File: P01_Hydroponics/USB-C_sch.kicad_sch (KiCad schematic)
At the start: 24 parts, among them J7 USB_C_Receptacle_USB2.0_16P, Q3 PMOS, Q4 PMOS

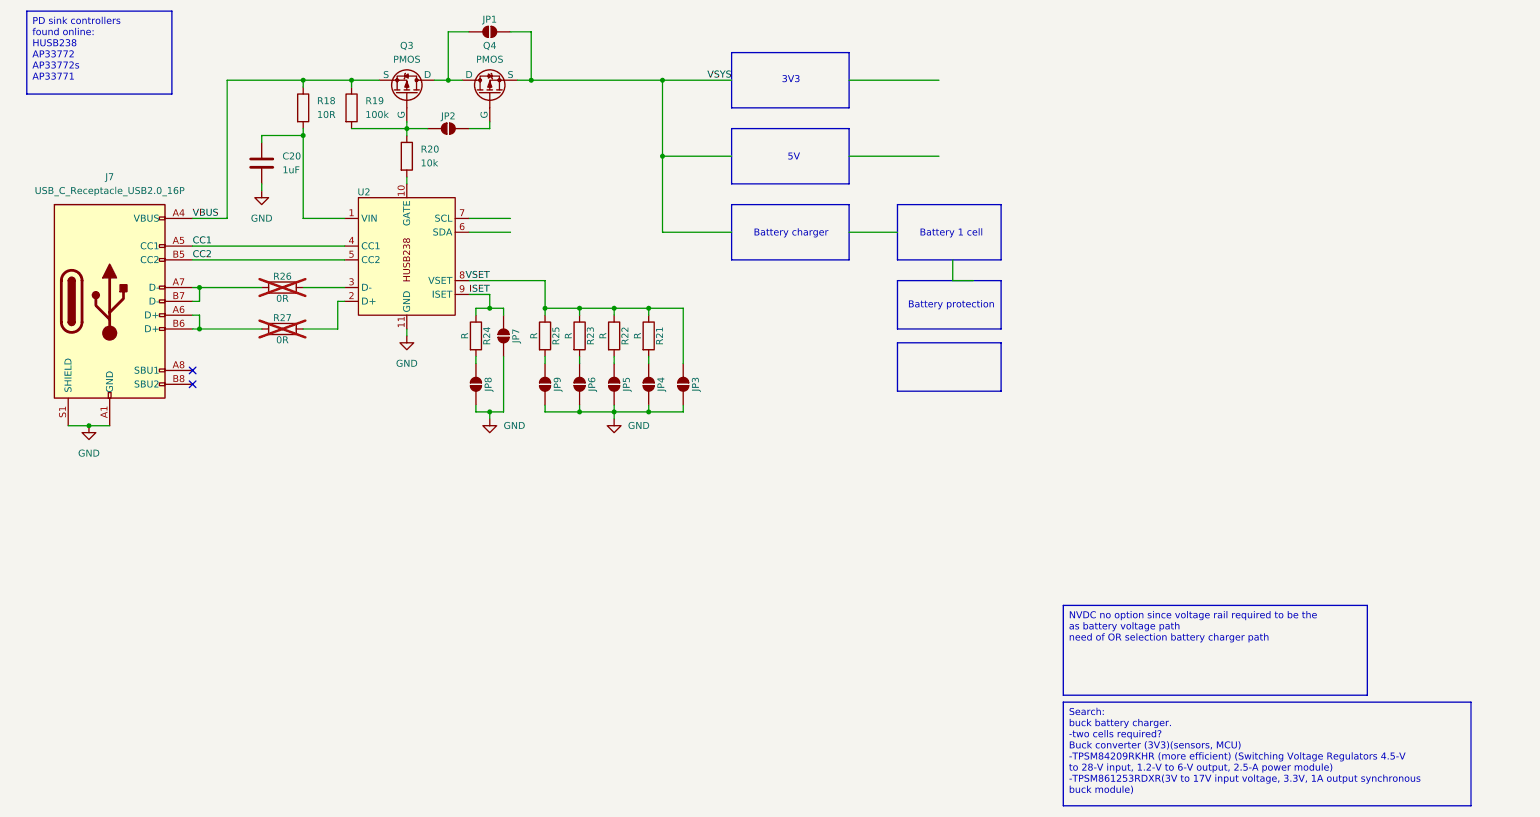
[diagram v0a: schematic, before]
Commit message: New version
Modified PD sink controller, and added 3v3 and 5V DC-DC buck converters
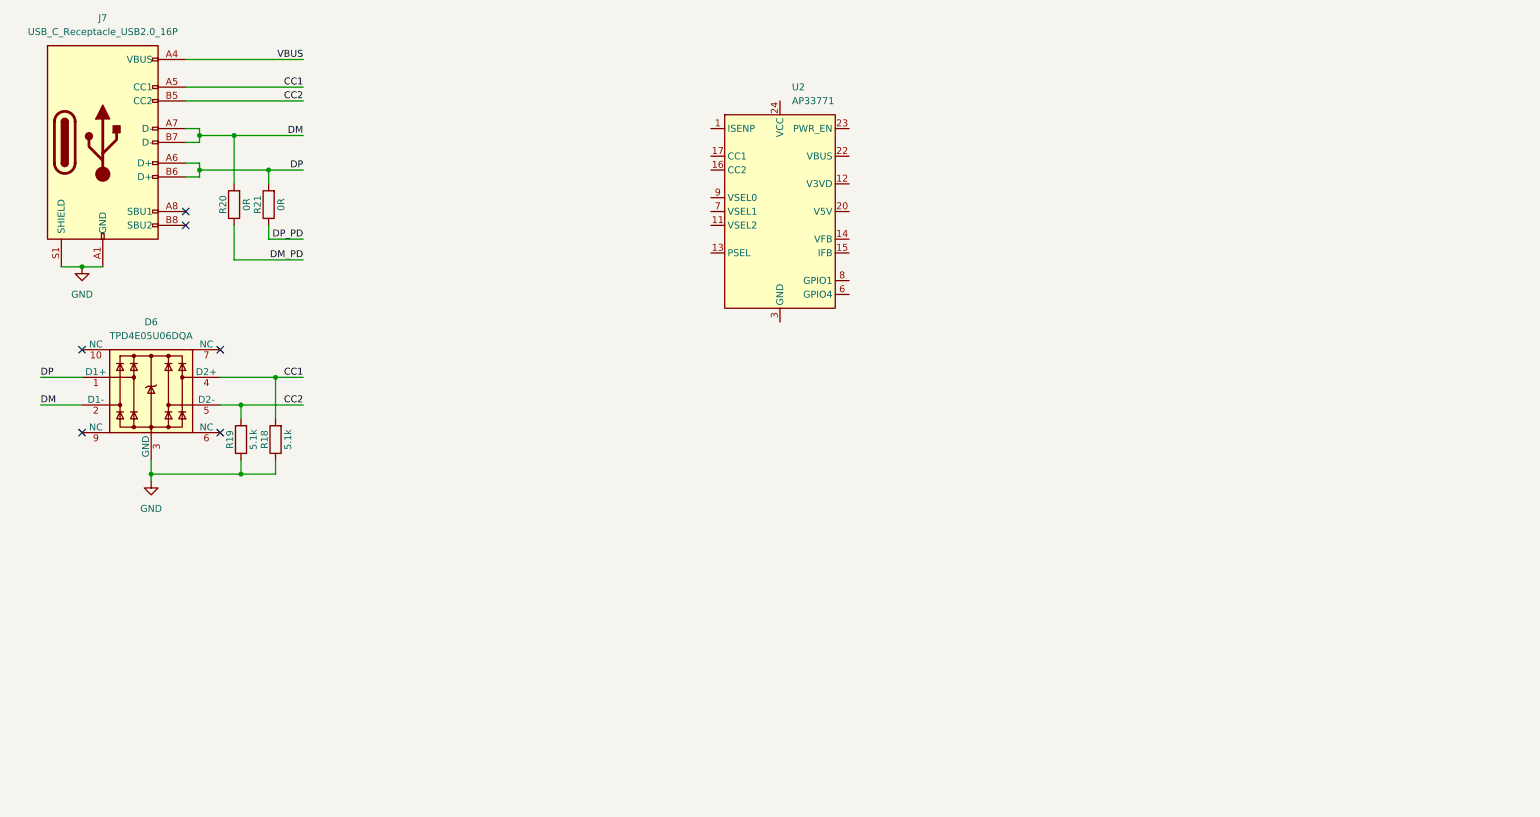
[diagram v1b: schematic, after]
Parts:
- removed C20: 1uF, symbol Device:C
- removed JP1, JP2, JP3, JP4, JP5, JP6, JP7, JP8, JP9: ~, symbol Jumper:SolderJumper_2_Open
- removed Q3, Q4: PMOS, symbol Simulation_SPICE:PMOS
- removed R22, R23, R24, R25: R, symbol Device:R
- removed R26, R27: 0R, symbol Device:R
- removed U2: ~, Package_DFN_QFN:DFN-10-1EP_3x3mm_P0.5mm_EP1.55x2.48mm, symbol USB_Type-C_PD:HUSB238
- added D6: TPD4E05U06DQA, Package_SON:USON-10_2.5x1.0mm_P0.5mm, symbol Power_Protection:TPD4E05U06DQA
- added U2: AP33771, Package_DFN_QFN:QFN-24-1EP_4x4mm_P0.5mm_EP2.7x2.7mm, symbol Interface_USB:AP33771
- R18: value 10R -> 5.1k
- R19: value 100k -> 5.1k
- R20: value 10k -> 0R
- R21: value R -> 0R
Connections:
- net CC1: now also R18.2, D6.4 (D2+)
- net CC2: now also R19.2, D6.5 (D2-)
- net GND: now also R18.1, R19.1, D6.3 (GND), D6.8 (GND)
- net VBUS: no longer R18.1, R19.1
- net DM_PD: now reaches R20.1
- net DM_PD: no longer R19.2
- net DP: now reaches R21.2
- net DP: now also J7.A6 (D+), J7.B6 (D+), D6.1 (D1+)
- net DM: now reaches J7.A7 (D-), J7.B7 (D-)
- net DM: now also R20.2, D6.2 (D1-)
- net VSET renamed DP_PD
- new net: U2.25 (GND), U2.3 (GND)
- no-connect marks 2 -> 6
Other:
- note removed: "3V3"
- note removed: "5V"
- note removed: "Battery 1 cell"
- note removed: "Battery charger"
- note removed: "Battery protection"
- moved on the sheet: J7
